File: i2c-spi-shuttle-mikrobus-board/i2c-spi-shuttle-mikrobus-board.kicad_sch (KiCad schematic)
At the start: 14 parts, among them J1 Conn_01x08, J2 Conn_01x08, J3 Shuttle, SW1 ADDR, U1 SC18IS606PW, U2 PCAL9538APW

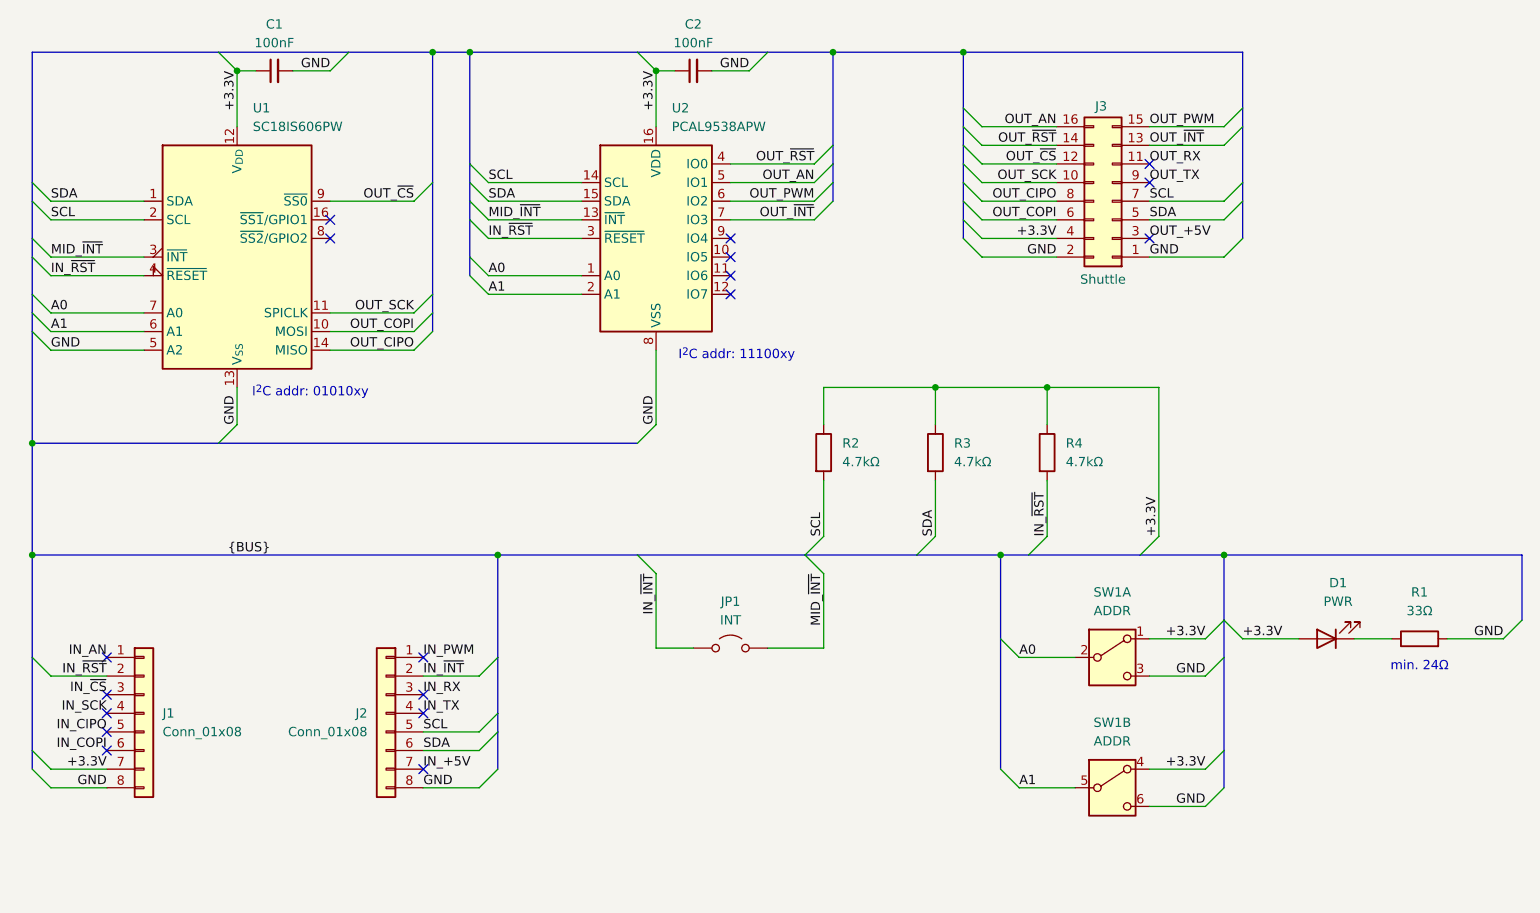
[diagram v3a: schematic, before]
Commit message: annotate schematic & board, pass +5V, update constraints
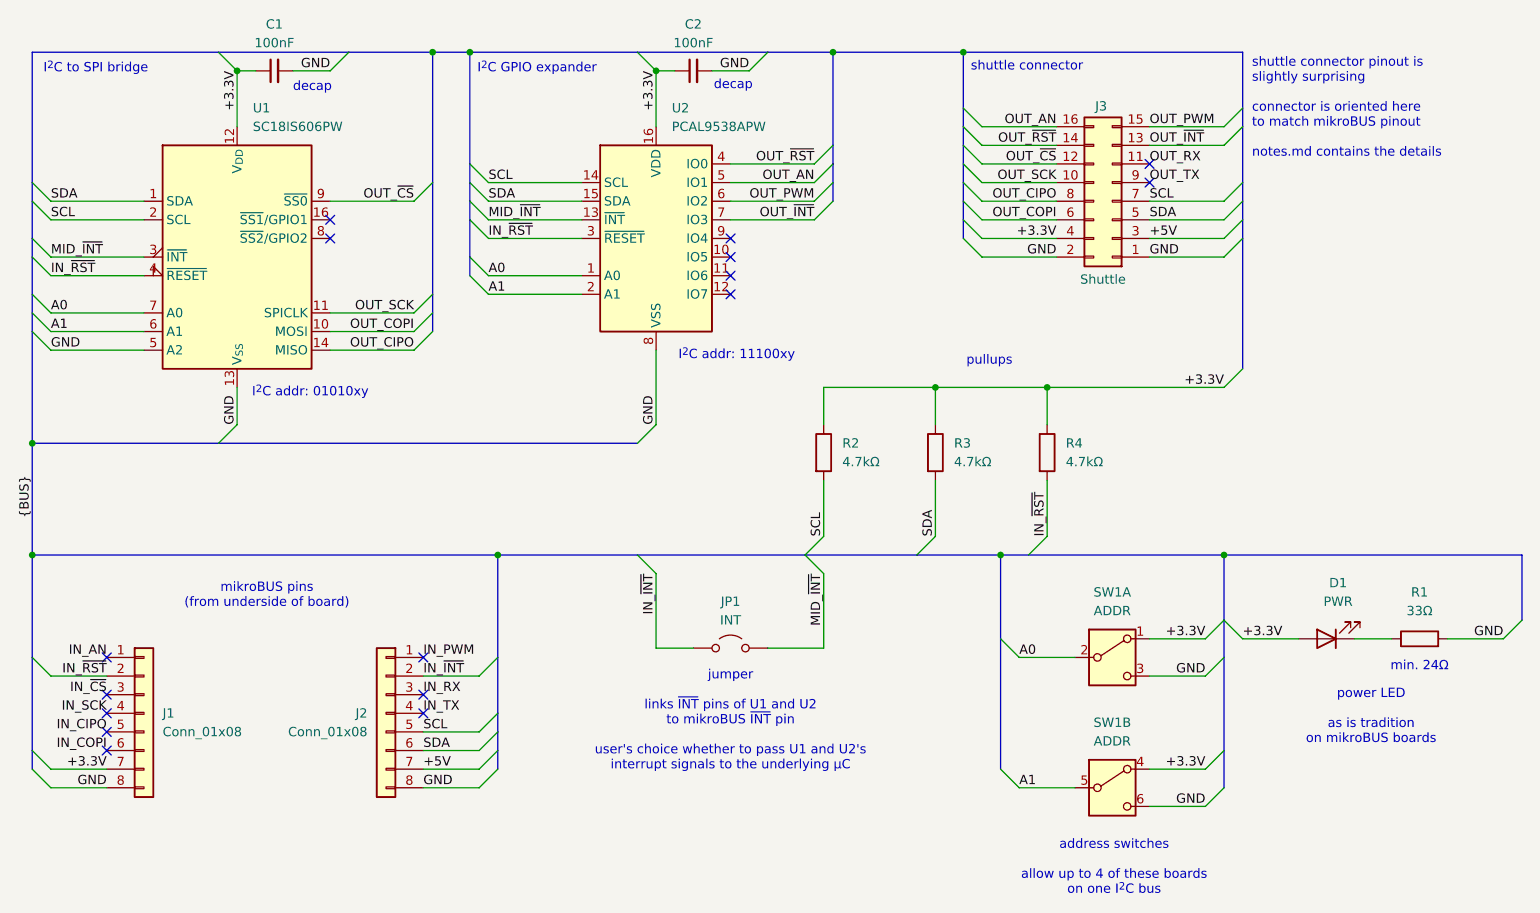
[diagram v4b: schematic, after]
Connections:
- net OUT_+5V is gone; now on net +5V: J3.3 (Pin_3)
- net IN_+5V renamed +5V
- no-connect marks 18 -> 16
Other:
- note added: "I^{2}C GPIO expander"
- note added: "I^{2}C to SPI bridge"
- note added: "address switches allow up to 4 of these boards on one I^{2}C bus"
- note added: "decap"
- note added: "jumper links ~{INT} pins of U1 and U2 to mikroBUS ~{INT} pin user's choice whether to pass U1 and U2's interrupt signals to the underlying µC"
- note added: "mikroBUS pins (from underside of board)"
- note added: "power LED as is tradition on mikroBUS boards"
- note added: "pullups"
- note added: "shuttle connector"
- note added: "shuttle connector pinout is slightly surprising connector is oriented here to match mikroBUS pinout notes.md contains the details"
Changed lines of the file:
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@@
+		)
+	)
+	(text "address switches\n\nallow up to 4 of these boards\non one I^{2}C bus"
+		(exclude_from_sim no)
+		(at 197.104 154.432 0)
+		(effects
+			(font
+				(size 1.27 1.27)
+			)
+			(justify top)
+		)
+	)
+	(text "power LED\n\nas is tradition\non mikroBUS boards"
+		(exclude_from_sim no)
+		(at 232.156 133.858 0)
+		(effects
+			(font
+				(size 1.27 1.27)
+			)
+			(justify top)
+		)
+	)
+	(text "I^{2}C GPIO expander"
+		(exclude_from_sim no)
+		(at 110.236 48.514 0)
+		(effects
+			(font
+				(size 1.27 1.27)
+			)
+			(justify left top)
 		)
 	)
@@
 				(size 1.27 1.27)
 			)
+		)
+	)
+	(text "I^{2}C to SPI bridge"
+		(exclude_from_sim no)
+		(at 51.054 48.514 0)
+		(effects
+			(font
+				(size 1.27 1.27)
+			)
+			(justify left top)
+		)
+	)
+	(text "shuttle connector pinout is\nslightly surprising\n\nconnector is oriented here\nto match mikroBUS pinout\n\nnotes.md contains the details"
+		(exclude_from_sim no)
+		(at 215.9 47.752 0)
+		(effects
+			(font
+				(size 1.27 1.27)
+			)
+			(justify left top)
+		)
+	)
+	(text "decap"
+		(exclude_from_sim no)
+		(at 85.09 51.054 0)
+		(effects
+			(font
+				(size 1.27 1.27)
+			)
+			(justify left top)
+		)
+	)
+	(text "jumper\n\nlinks ~{INT} pins of U1 and U2\nto mikroBUS ~{INT} pin\n\nuser's choice whether to pass U1 and U2's\ninterrupt signals to the underlying µC"
+		(exclude_from_sim no)
+		(at 144.78 131.318 0)
+		(effects
+			(font
+				(size 1.27 1.27)
+			)
+			(justify top)
+		)
+	)
+	(text "mikroBUS pins\n(from underside of board)"
+		(exclude_from_sim no)
+		(at 81.534 119.38 0)
+		(effects
+			(font
+				(size 1.27 1.27)
+			)
+			(justify top)
+		)
+	)
+	(text "decap"
+		(exclude_from_sim no)
+		(at 142.494 50.8 0)
+		(effects
+			(font
+				(size 1.27 1.27)
+			)
+			(justify left top)
+		)
+	)
+	(text "pullups"
+		(exclude_from_sim no)
+		(at 180.086 88.392 0)
+		(effects
+			(font
+				(size 1.27 1.27)
+			)
+			(justify top)
+		)
+	)
+	(text "shuttle connector"
+		(exclude_from_sim no)
+		(at 177.546 48.26 0)
+		(effects
+			(font
+				(size 1.27 1.27)
+			)
+			(justify left top)
 		)
 	)
@@
 	)
 	(no_connect
-		(at 201.93 72.39)
-	)
-	(no_connect
-		(at 102.87 144.78)
-	)
-	(no_connect
 		(at 102.87 134.62)
 	)
@@
 	)
 	(bus_entry
+		(at 113.03 142.24)
+		(size -2.54 2.54)
+		(stroke
+			(width 0)
+			(type default)
+		)
+	)
+	(bus_entry
+		(at 214.63 69.85)
+		(size -2.54 2.54)
+		(stroke
+			(width 0)
+			(type default)
+		)
+	)
+	(bus_entry
 		(at 214.63 57.15)
 		(size -2.54 2.54)
@@
 	)
 	(bus_entry
-		(at 200.66 115.57)
-		(size 2.54 -2.54)
-		(stroke
-			(width 0)
-			(type default)
-		)
-	)
-	(bus_entry
 		(at 132.08 46.99)
 		(size 2.54 2.54)
@@
 	)
 	(bus_entry
+		(at 212.09 92.71)
+		(size 2.54 -2.54)
+		(stroke
+			(width 0)
+			(type default)
+		)
+	)
+	(bus_entry
 		(at 104.14 64.77)
 		(size -2.54 2.54)
@@
 	(bus
 		(pts
+			(xy 214.63 69.85) (xy 214.63 72.39)
+		)
+		(stroke
+			(width 0)
+			(type default)
+		)
+	)
+	(bus
+		(pts
 			(xy 49.53 100.33) (xy 74.93 100.33)
 		)
@@
 	(wire
 		(pts
+			(xy 187.96 92.71) (xy 212.09 92.71)
+		)
+		(stroke
+			(width 0)
+			(type default)
+		)
+	)
+	(wire
+		(pts
 			(xy 90.17 87.63) (xy 101.6 87.63)
 		)
@@
 	(bus
 		(pts
-			(xy 113.03 139.7) (xy 113.03 144.78)
-		)
-		(stroke
-			(width 0)
-			(type default)
-		)
-	)
-	(bus
-		(pts
-			(xy 185.42 115.57) (xy 200.66 115.57)
+			(xy 113.03 139.7) (xy 113.03 142.24)
+		)
+		(stroke
+			(width 0)
+			(type default)
+		)
+	)
+	(bus
+		(pts
+			(xy 185.42 115.57) (xy 212.09 115.57)
 		)
 		(stroke
@@
 	(wire
 		(pts
+			(xy 102.87 144.78) (xy 110.49 144.78)
+		)
+		(stroke
+			(width 0)
+			(type default)
+		)
+	)
+	(wire
+		(pts
 			(xy 111.76 80.01) (xy 124.46 80.01)
 		)
@@
 	(bus
 		(pts
-			(xy 214.63 67.31) (xy 214.63 72.39)
+			(xy 214.63 67.31) (xy 214.63 69.85)
 		)
 		(stroke
@@
 		)
 	)
-	(bus
-		(pts
-			(xy 200.66 115.57) (xy 212.09 115.57)
-		)
-		(stroke
-			(width 0)
-			(type default)
-		)
-	)
 	(wire
 		(pts
@@
 	(bus
 		(pts
+			(xy 214.63 72.39) (xy 214.63 90.17)
+		)
+		(stroke
+			(width 0)
+			(type default)
+		)
+	)
+	(bus
+		(pts
 			(xy 176.53 64.77) (xy 176.53 67.31)
 		)
@@
 		)
 	)
-	(wire
-		(pts
-			(xy 203.2 113.03) (xy 203.2 92.71)
-		)
-		(stroke
-			(width 0)
-			(type default)
-		)
-	)
 	(bus
 		(pts
@@
 	(bus
 		(pts
+			(xy 113.03 142.24) (xy 113.03 144.78)
+		)
+		(stroke
+			(width 0)
+			(type default)
+		)
+	)
+	(bus
+		(pts
 			(xy 49.53 67.31) (xy 49.53 64.77)
 		)
@@
 		)
 	)
+	(wire
+		(pts
+			(xy 212.09 72.39) (xy 201.93 72.39)
+		)
+		(stroke
+			(width 0)
+			(type default)
+		)
+	)
 	(bus
 		(pts
@@
 		(pts
 			(xy 212.09 115.57) (xy 252.73 115.57)
-		)
-		(stroke
-			(width 0)
-			(type default)
-		)
-	)
-	(wire
-		(pts
-			(xy 203.2 92.71) (xy 187.96 92.71)
 		)
 		(stroke
@@
 	)
 	(label "+3.3V"
-		(at 203.2 113.03 90)
-		(effects
-			(font
-				(size 1.27 1.27)
-			)
-			(justify left bottom)
+		(at 212.09 92.71 180)
+		(effects
+			(font
+				(size 1.27 1.27)
+			)
+			(justify right bottom)
 		)
 	)
@@
 		)
 	)
-	(label "OUT_+5V"
+	(label "+5V"
 		(at 201.93 72.39 0)
 		(effects
@@
 	)
 	(label "{BUS}"
-		(at 76.2 115.57 0)
+		(at 49.53 110.49 90)
 		(effects
 			(font
@@
 		)
 	)
-	(label "IN_+5V"
+	(label "+5V"
 		(at 102.87 144.78 0)
 		(effects

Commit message: add LCSC numbers
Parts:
- C1, C2: LCSC (none) -> C307331
- D1: LCSC (none) -> C2297
- J1, J2, JP1: now left out of the parts list
- J3: LCSC (none) -> C5338669
- R1: LCSC (none) -> C23140
- R2, R3, R4: LCSC (none) -> C25900
- SW1: LCSC (none) -> C3664582
- U1: LCSC (none) -> C5190384
- U2: LCSC (none) -> C2652336
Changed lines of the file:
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@@
+			)
+		)
+		(property "LCSC" "C307331"
+			(at 139.7 49.53 90)
+			(effects
+				(font
+					(size 1.27 1.27)
+				)
+				(hide yes)
 			)
 		)
@@
 		(unit 1)
 		(exclude_from_sim no)
-		(in_bom yes)
+		(in_bom no)
 		(on_board yes)
 		(dnp no)
@@
 			)
 		)
+		(property "LCSC" "C3664582"
+			(at 196.85 147.32 0)
+			(effects
+				(font
+					(size 1.27 1.27)
+				)
+				(hide yes)
+			)
+		)
 		(pin "2"
 		)
@@
 			)
 		)
+		(property "LCSC" "C2297"
+			(at 226.06 127 0)
+			(effects
+				(font
+					(size 1.27 1.27)
+				)
+				(hide yes)
+			)
+		)
 		(pin "1"
 		)
@@
 			)
 		)
+		(property "LCSC" "C25900"
+			(at 187.96 101.6 0)
+			(effects
+				(font
+					(size 1.27 1.27)
+				)
+				(hide yes)
+			)
+		)
 		(pin "2"
 		)
@@
 			)
 		)
+		(property "LCSC" "C23140"
+			(at 238.76 127 90)
+			(effects
+				(font
+					(size 1.27 1.27)
+				)
+				(hide yes)
+			)
+		)
 		(pin "2"
 		)
@@
 		)
 		(property "Description" "Generic connector, double row, 02x08, odd/even pin numbering scheme (row 1 odd numbers, row 2 even numbers), script generated (kicad-library-utils/schlib/autogen/connector/)"
+			(at 196.85 67.31 0)
+			(effects
+				(font
+					(size 1.27 1.27)
+				)
+				(hide yes)
+			)
+		)
+		(property "LCSC" "C5338669"
 			(at 196.85 67.31 0)
 			(effects
@@
 			)
 		)
+		(property "LCSC" "C307331"
+			(at 82.55 49.53 90)
+			(effects
+				(font
+					(size 1.27 1.27)
+				)
+				(hide yes)
+			)
+		)
 		(pin "2"
 		)
@@
 			)
 		)
+		(property "LCSC" "C2652336"
+			(at 134.62 72.39 0)
+			(effects
+				(font
+					(size 1.27 1.27)
+				)
+				(hide yes)
+			)
+		)
 		(pin "13"
 		)
@@
 			)
 		)
+		(property "LCSC" "C5190384"
+			(at 77.47 74.93 0)
+			(effects
+				(font
+					(size 1.27 1.27)
+				)
+				(hide yes)
+			)
+		)
 		(pin "12"
 		)
@@
 			)
 		)
+		(property "LCSC" "C25900"
+			(at 157.48 101.6 0)
+			(effects
+				(font
+					(size 1.27 1.27)
+				)
+				(hide yes)
+			)
+		)
 		(pin "2"
 		)
@@
 			)
 		)
+		(property "LCSC" "C3664582"
+			(at 196.85 129.54 0)
+			(effects
+				(font
+					(size 1.27 1.27)
+				)
+				(hide yes)
+			)
+		)
 		(pin "2"
 		)
@@
 			)
 		)
+		(property "LCSC" "C25900"
+			(at 172.72 101.6 0)
+			(effects
+				(font
+					(size 1.27 1.27)
+				)
+				(hide yes)
+			)
+		)
 		(pin "2"
 		)
@@
 		(unit 1)
 		(exclude_from_sim no)
-		(in_bom yes)
+		(in_bom no)
 		(on_board yes)
 		(dnp no)
@@
 		(unit 1)
 		(exclude_from_sim no)
-		(in_bom yes)
-		(on_board yes)
-		(dnp no)
+		(in_bom no)
+		(on_board yes)
+		(dnp no)
